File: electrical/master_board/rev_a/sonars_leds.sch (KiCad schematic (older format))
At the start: 9 parts, among them CN101 BRIDGE_NE_INNER;3xM1x1+M1x5, CN102 BRIDGE_NW_INNER;M1x2+M2x5, CN103 BRIDGE_SE_INNER;M1x8, CN104 BRIDGE_SW_INNER;M1x8, CN50 HCSR04;F1X4, CN51 HCSR04LP;F1X4, CN52 HCSR04LP;F1X4, CN53 HCSR04LP;F1X4, CN54 HCSR04LP;F1X4

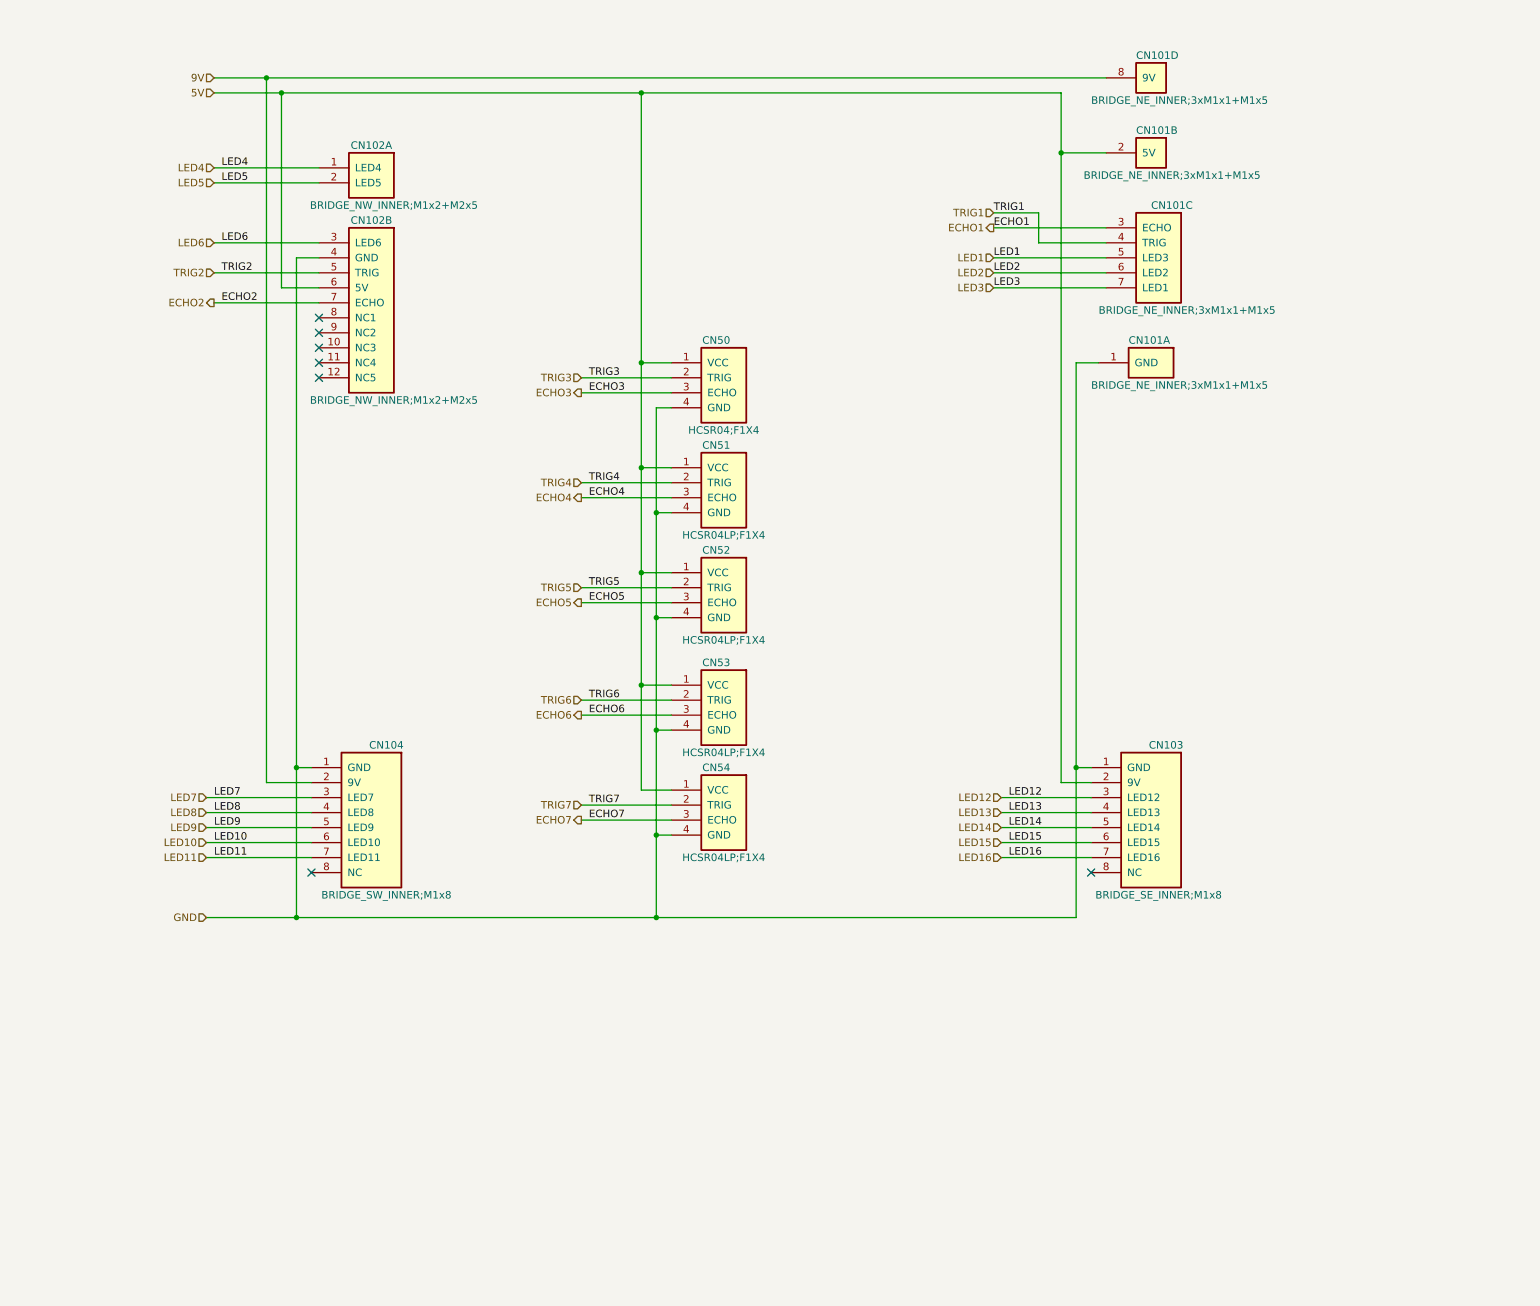
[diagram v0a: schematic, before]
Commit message: Added level shifting to Sonars.  Added shift register for LED's.
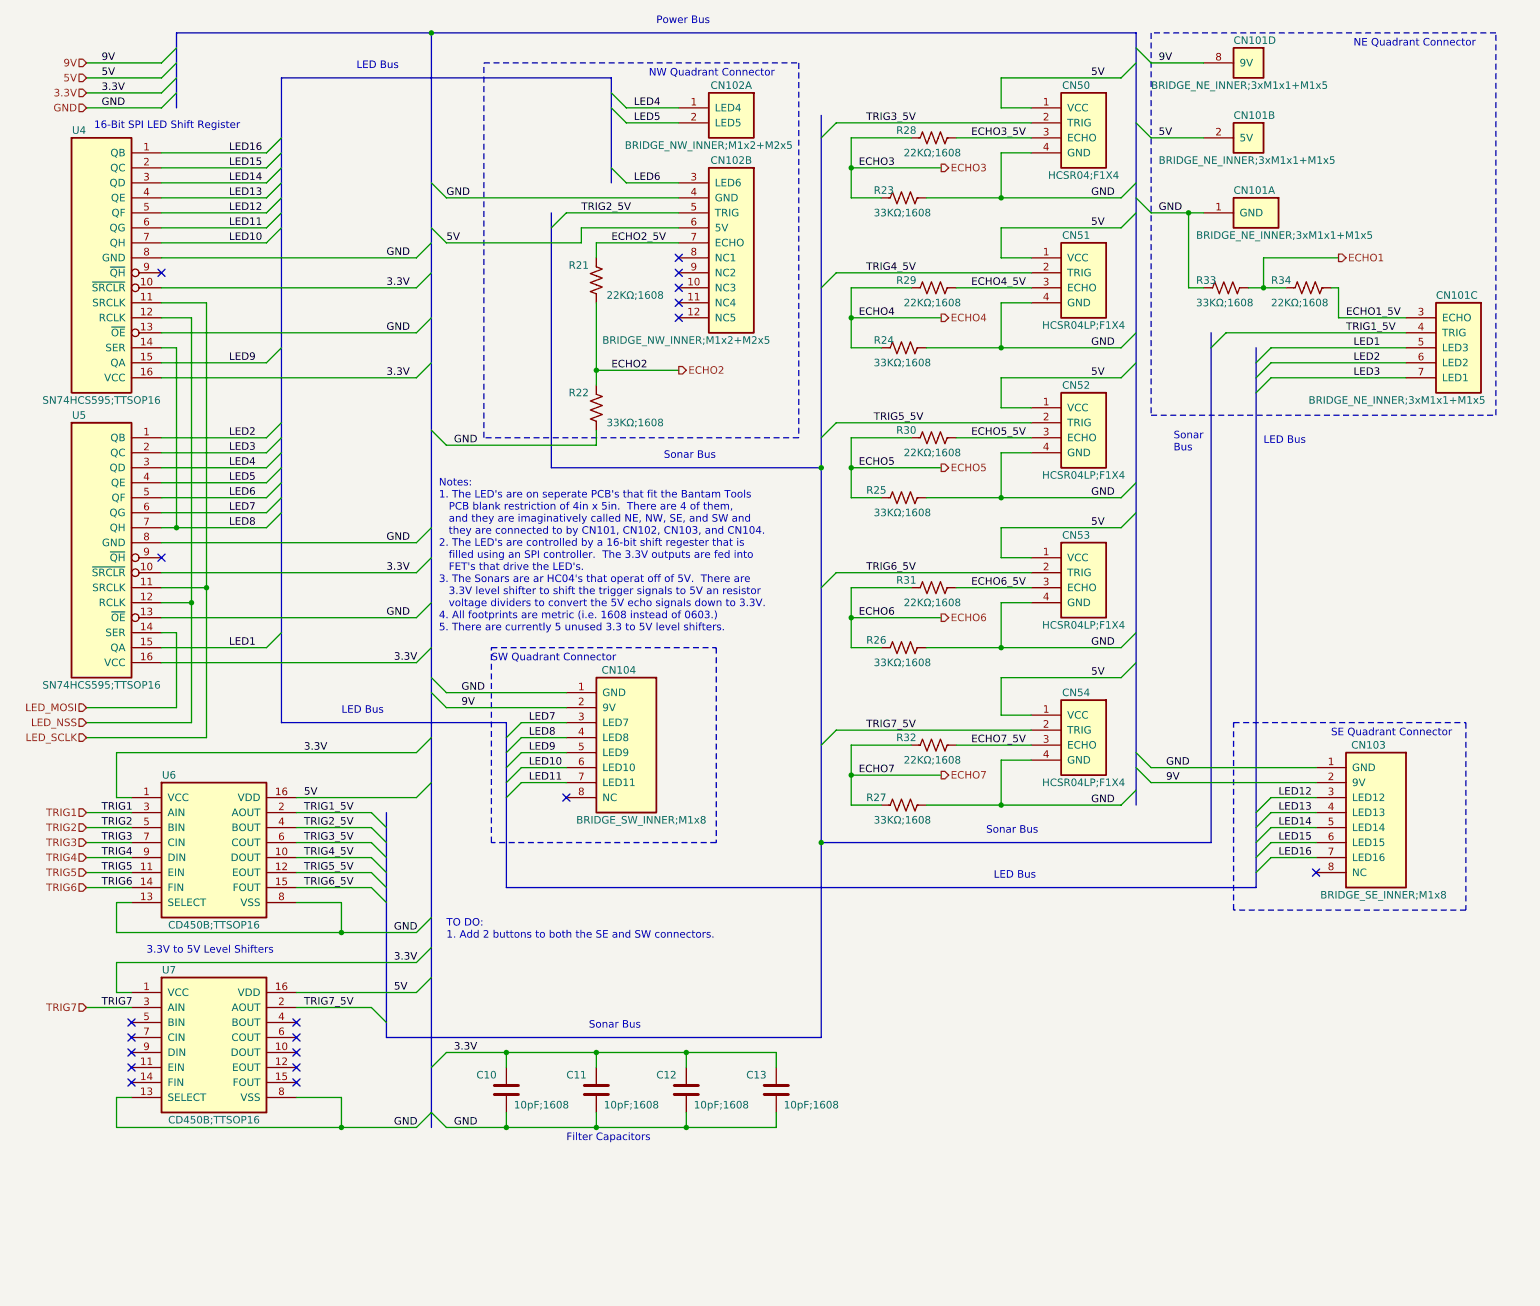
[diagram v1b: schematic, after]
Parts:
- added C10, C11, C12, C13: 10pF;1608, symbol Device:C
- added R21, R28, R29, R30, R31, R32, R34: 22KΩ;1608, symbol Device:R_US
- added R22, R23, R24, R25, R26, R27, R33: 33KΩ;1608, symbol Device:R_US
- added U4, U5: SN74HCS595;TTSOP16, Package_SO:TSSOP-16_4.4x5mm_P0.65mm, symbol HR2:SN74HCS595;TTSOP16
- added U6, U7: CD450B;TTSOP16, Package_SO:TSSOP-16_4.4x5mm_P0.65mm, symbol HR2:CD450B;TTSOP16
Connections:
- net 5V: now also U6.16 (VDD), U7.16 (VDD); no longer CN103.2 (9V)
- net 9V: now also CN103.2 (9V)
- net ECHO1: now also R33.1, R34.2; no longer CN101.3 (ECHO)
- net ECHO2: now also R21.1, R22.2; no longer CN102.7 (ECHO)
- net ECHO3: now also R23.2, R28.2; no longer CN50.3 (ECHO)
- net ECHO4: now also R24.2, R29.2; no longer CN51.3 (ECHO)
- net ECHO5: now also R25.2, R30.2; no longer CN52.3 (ECHO)
- net ECHO6: now also R26.2, R31.2; no longer CN53.3 (ECHO)
- net ECHO7: now also R27.2, R32.2; no longer CN54.3 (ECHO)
- net GND: now also C10.2, C11.2, C12.2, C13.2, R22.1, R23.1, R24.1, R25.1, R26.1, R27.1, R33.2, U4.13 (~OE), U4.8 (GND), U5.13 (~OE), U5.8 (GND), U6.13 (SELECT), U6.8 (VSS), U7.13 (SELECT), U7.8 (VSS)
- net LED1: now also U5.15 (QA)
- net LED10: now also U4.7 (QH)
- net LED11: now also U4.6 (QG)
- net LED12: now also U4.5 (QF)
- net LED13: now also U4.4 (QE)
- net LED14: now also U4.3 (QD)
- net LED15: now also U4.2 (QC)
- net LED16: now also U4.1 (QB)
- net LED2: now also U5.1 (QB)
- net LED3: now also U5.2 (QC)
- net LED4: now also U5.3 (QD)
- net LED5: now also U5.4 (QE)
- net LED6: now also U5.5 (QF)
- net LED7: now also U5.6 (QG)
- net LED8: now also U4.14 (SER), U5.7 (QH)
- net LED9: now also U4.15 (QA)
- net TRIG1: now also U6.3 (AIN); no longer CN101.4 (TRIG)
- net TRIG2: now also U6.5 (BIN); no longer CN102.5 (TRIG)
- net TRIG3: now also U6.7 (CIN); no longer CN50.2 (TRIG)
- net TRIG4: now also U6.9 (DIN); no longer CN51.2 (TRIG)
- net TRIG5: now also U6.11 (EIN); no longer CN52.2 (TRIG)
- net TRIG6: now also U6.14 (FIN); no longer CN53.2 (TRIG)
- net TRIG7: now also U7.3 (AIN); no longer CN54.2 (TRIG)
- new net 3.3V: C10.1, C11.1, C12.1, C13.1, U4.10 (~SRCLR), U4.16 (VCC), U5.10 (~SRCLR), U5.16 (VCC), U6.1 (VCC), U7.1 (VCC)
- new net ECHO1_5V: CN101.3 (ECHO), R34.1
- new net ECHO2_5V: CN102.7 (ECHO), R21.2
- new net ECHO3_5V: CN50.3 (ECHO), R28.1
- new net ECHO4_5V: CN51.3 (ECHO), R29.1
- new net ECHO5_5V: CN52.3 (ECHO), R30.1
- new net ECHO6_5V: CN53.3 (ECHO), R31.1
- new net ECHO7_5V: CN54.3 (ECHO), R32.1
- new net LED_MOSI: U5.14 (SER)
- new net LED_NSS: U4.12 (RCLK), U5.12 (RCLK)
- new net LED_SCLK: U4.11 (SRCLK), U5.11 (SRCLK)
- new net TRIG1_5V: CN101.4 (TRIG), U6.2 (AOUT)
- new net TRIG2_5V: CN102.5 (TRIG), U6.4 (BOUT)
- new net TRIG3_5V: CN50.2 (TRIG), U6.6 (COUT)
- new net TRIG4_5V: CN51.2 (TRIG), U6.10 (DOUT)
- new net TRIG5_5V: CN52.2 (TRIG), U6.12 (EOUT)
- new net TRIG6_5V: CN53.2 (TRIG), U6.15 (FOUT)
- new net TRIG7_5V: CN54.2 (TRIG), U7.2 (AOUT)
- no-connect marks 7 -> 19
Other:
- note added: "16-Bit SPI LED Shift Register"
- note added: "3.3V to 5V Level Shifters"
- note added: "Filter Capacitors"
- note added: "LED Bus"
- note added: "NE Quadrant Connector"
- note added: "NW Quadrant Connector"
- note added: "Notes:\n1. The LED's are on seperate PCB's that fit the Bantam Tools\n PCB blank restriction of 4in x 5in. There are 4 of them,\n and they are imaginatively called NE, NW, SE, and SW and\n they are connected to by CN101, CN102, CN103, and CN104.\n2. The LED's are controlled by a 16-bit shift regester that is\n filled using an SPI controller. The 3.3V outputs are fed into\n FET's that drive the LE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"
- note added: "Power Bus"
- note added: "SE Quadrant Connector"
- note added: "SW Quadrant Connector"
- note added: "Sonar Bus"
- note added: "Sonar\nBus"
- note added: "TO DO:\n1. Add 2 buttons to both the SE and SW connectors."
- moved on the sheet: CN101A, CN101B, CN101C, CN101D, CN102A, CN102B, CN103, CN104, CN50, CN51, CN52, CN53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

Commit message: Added servo connectors.
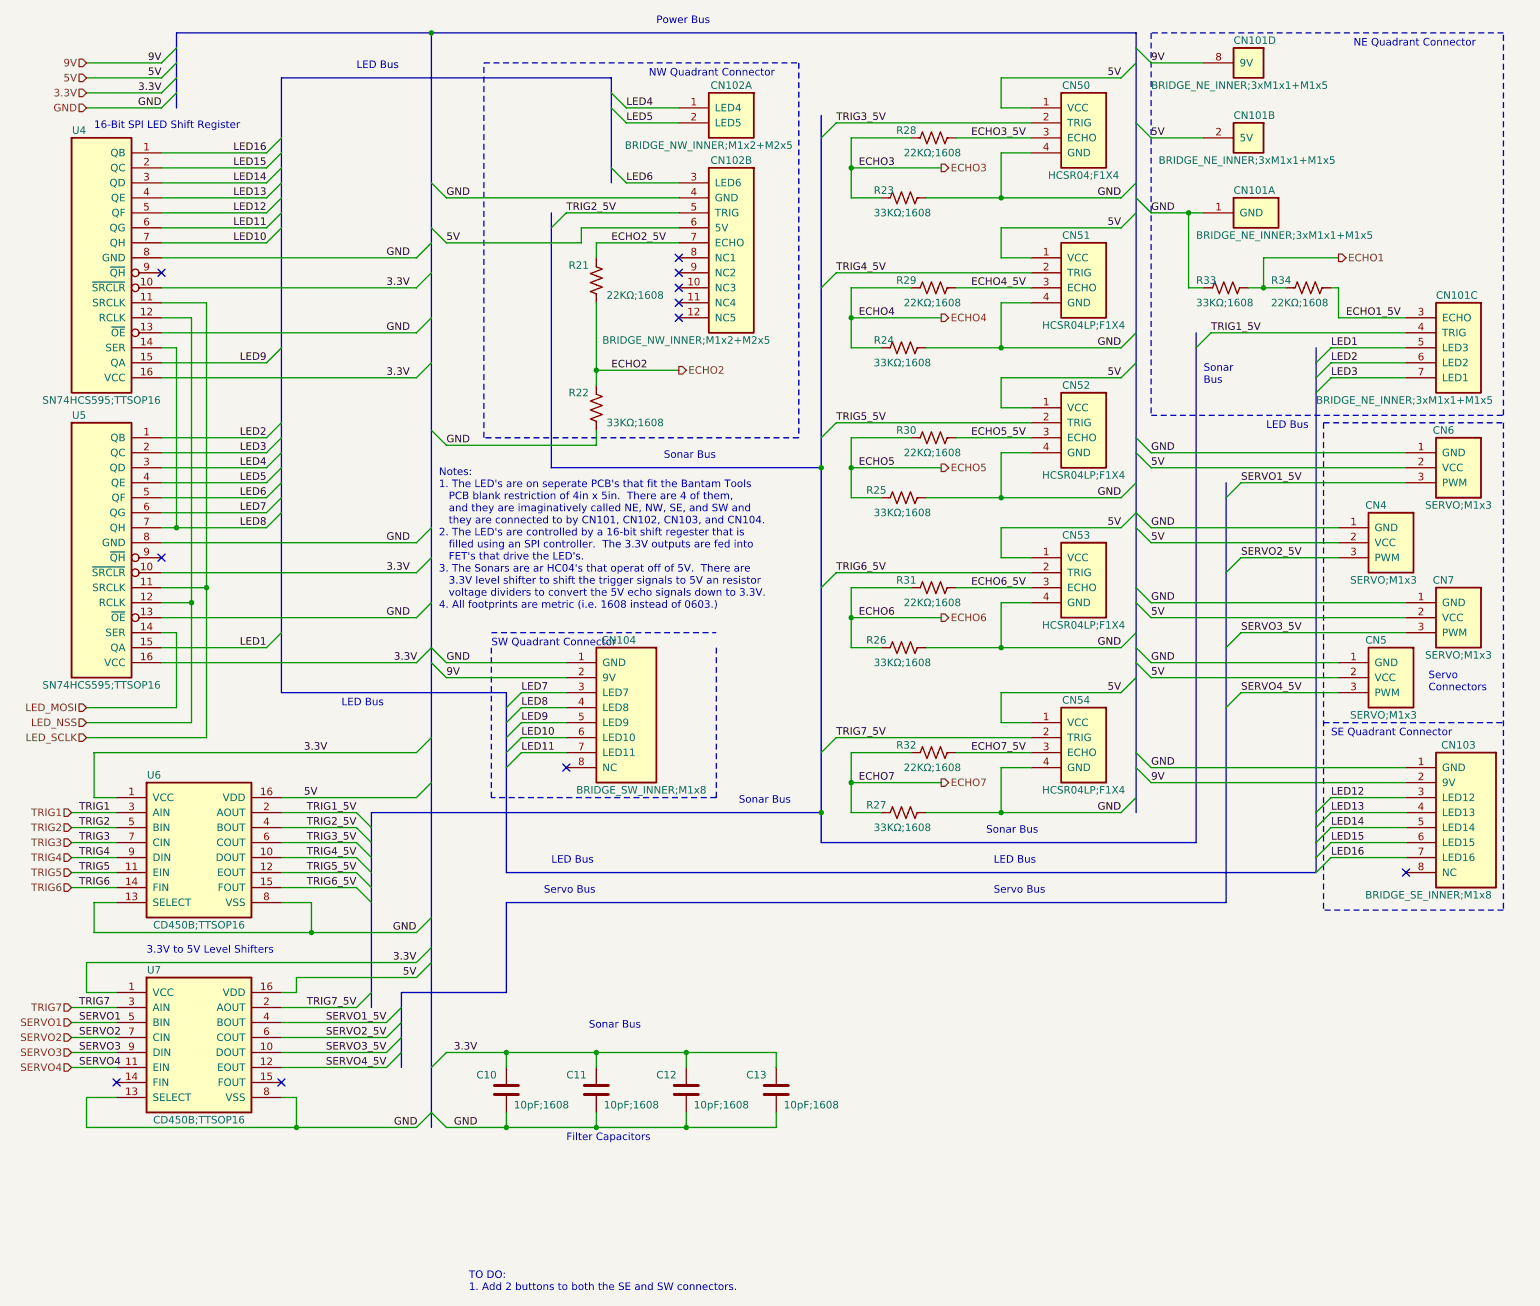
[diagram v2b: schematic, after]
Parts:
- added CN4, CN5, CN6, CN7: SERVO;M1x3, Connector_PinHeader_2.54mm:PinHeader_1x03_P2.54mm_Vertical, symbol HR2:SERVO;M1x3
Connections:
- net 5V: now also CN4.2 (VCC), CN5.2 (VCC), CN6.2 (VCC), CN7.2 (VCC)
- net GND: now also CN4.1 (GND), CN5.1 (GND), CN6.1 (GND), CN7.1 (GND)
- net SERVO3_5V: now reaches U7.10 (DOUT)
- net SERVO3_5V: now also CN7.3 (PWM)
- net SERVO4: now reaches U7.11 (EIN)
- net SERVO4_5V: now reaches U7.12 (EOUT)
- net SERVO4_5V: now also CN5.3 (PWM)
- net SERVO1_5V: now reaches U7.4 (BOUT)
- net SERVO1_5V: now also CN6.3 (PWM)
- net SERVO1: now reaches U7.5 (BIN)
- net SERVO2_5V: now reaches U7.6 (COUT)
- net SERVO2_5V: now also CN4.3 (PWM)
- net SERVO2: now reaches U7.7 (CIN)
- net SERVO3: now reaches U7.9 (DIN)
- no-connect marks 19 -> 11
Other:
- note added: "Servo Bus"
- note added: "Servo\nConnectors"
- moved on the sheet: CN103, CN104, CN54, R27, R32, U6, U7
